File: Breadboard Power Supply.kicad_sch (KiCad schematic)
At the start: 29 parts, among them J1 USB-C, J10 Conn_01x02_Male, J11 Conn_01x02_Male, J2 Conn_02x03_Odd_Even, J3 Conn_02x03_Odd_Even, J8 Conn_01x02_Male, J9 Conn_01x02_Male, U1 LM1117-1.8, U2 LM1117-3.3

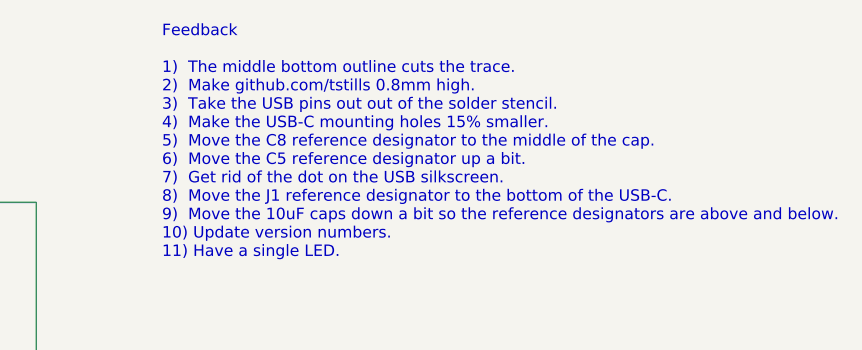
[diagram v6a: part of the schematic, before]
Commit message: Made the font for github.com/tstills larger.
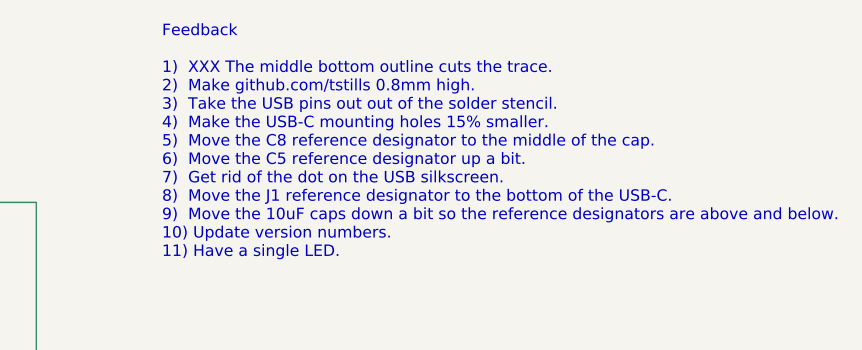
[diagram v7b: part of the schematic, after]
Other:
- note added: "Feedback 1) XXX The middle bottom outline cuts the trace. 2) Make github.com/tstills 0.8mm high. 3) Take the USB pins out out of the solder stencil. 4) Make the USB-C mounting holes 15% smaller. 5) Move the C8 reference designator to the middle of the cap. 6) Move the C5 reference designator up a bit. 7) Get rid of the dot on the USB silkscreen. 8) Move the J1 reference designator to the bottom o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"
- note removed: "Feedback 1) The middle bottom outline cuts the trace. 2) Make github.com/tstills 0.8mm high. 3) Take the USB pins out out of the solder stencil. 4) Make the USB-C mounting holes 15% smaller. 5) Move the C8 reference designator to the middle of the cap. 6) Move the C5 reference designator up a bit. 7) Get rid of the dot on the USB silkscreen. 8) Move the J1 reference designator to the bottom of th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"
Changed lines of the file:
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@@
     (effects (font (size 1.27 1.27)) (justify left bottom))
   )
-  (text "Feedback\n\n1)  The middle bottom outline cuts the trace.\n2)  Make github.com/tstills 0.8mm high.\n3)  Take the USB pins out out of the solder stencil.\n4)  Make the USB-C mounting holes 15% smaller.\n5)  Move the C8 reference designator to the middle of the cap.\n6)  Move the C5 reference designator up a bit.\n7)  Get rid of the dot on the USB silkscreen.\n8)  Move the J1 reference designator to the bottom of the USB-C.\n9)  Move the 10uF caps down a bit so the reference designators are above and below.\n10) Update version numbers.\n11) Have a single LED."
+  (text "Feedback\n\n1)  XXX The middle bottom outline cuts the trace.\n2)  Make github.com/tstills 0.8mm high.\n3)  Take the USB pins out out of the solder stencil.\n4)  Make the USB-C mounting holes 15% smaller.\n5)  Move the C8 reference designator to the middle of the cap.\n6)  Move the C5 reference designator up a bit.\n7)  Get rid of the dot on the USB silkscreen.\n8)  Move the J1 reference designator to the bottom of the USB-C.\n9)  Move the 10uF caps down a bit so the reference designators are above and below.\n10) Update version numbers.\n11) Have a single LED."
     (at 177.8 41.91 0)
     (effects (font (size 1.27 1.27)) (justify left bottom))

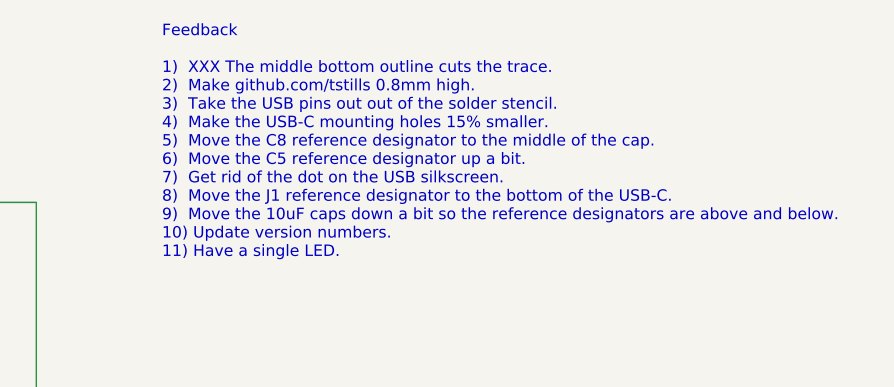
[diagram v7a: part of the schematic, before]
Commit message: Made the USB mounting holes 10% smaller.
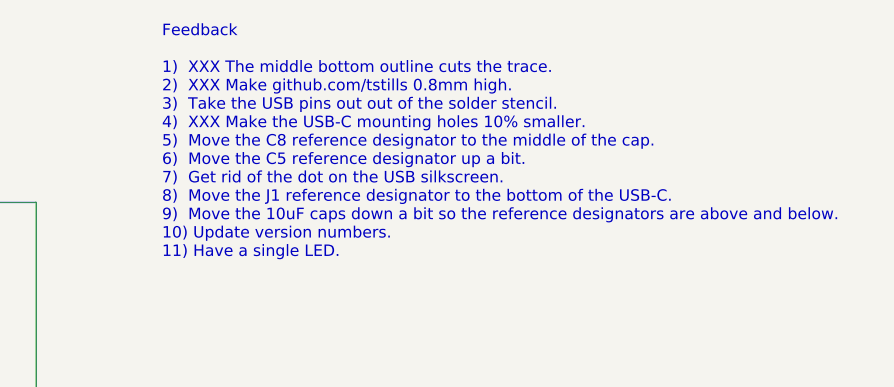
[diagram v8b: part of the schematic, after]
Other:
- note added: "Feedback 1) XXX The middle bottom outline cuts the trace. 2) XXX Make github.com/tstills 0.8mm high. 3) Take the USB pins out out of the solder stencil. 4) XXX Make the USB-C mounting holes 10% smaller. 5) Move the C8 reference designator to the middle of the cap. 6) Move the C5 reference designator up a bit. 7) Get rid of the dot on the USB silkscreen. 8) Move the J1 reference designator to the 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"
- note removed: "Feedback 1) XXX The middle bottom outline cuts the trace. 2) Make github.com/tstills 0.8mm high. 3) Take the USB pins out out of the solder stencil. 4) Make the USB-C mounting holes 15% smaller. 5) Move the C8 reference designator to the middle of the cap. 6) Move the C5 reference designator up a bit. 7) Get rid of the dot on the USB silkscreen. 8) Move the J1 reference designator to the bottom o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"
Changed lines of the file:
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@@
     (effects (font (size 1.27 1.27)) (justify left bottom))
   )
-  (text "Feedback\n\n1)  XXX The middle bottom outline cuts the trace.\n2)  Make github.com/tstills 0.8mm high.\n3)  Take the USB pins out out of the solder stencil.\n4)  Make the USB-C mounting holes 15% smaller.\n5)  Move the C8 reference designator to the middle of the cap.\n6)  Move the C5 reference designator up a bit.\n7)  Get rid of the dot on the USB silkscreen.\n8)  Move the J1 reference designator to the bottom of the USB-C.\n9)  Move the 10uF caps down a bit so the reference designators are above and below.\n10) Update version numbers.\n11) Have a single LED."
+  (text "Feedback\n\n1)  XXX The middle bottom outline cuts the trace.\n2)  XXX Make github.com/tstills 0.8mm high.\n3)  Take the USB pins out out of the solder stencil.\n4)  XXX Make the USB-C mounting holes 10% smaller.\n5)  Move the C8 reference designator to the middle of the cap.\n6)  Move the C5 reference designator up a bit.\n7)  Get rid of the dot on the USB silkscreen.\n8)  Move the J1 reference designator to the bottom of the USB-C.\n9)  Move the 10uF caps down a bit so the reference designators are above and below.\n10) Update version numbers.\n11) Have a single LED."
     (at 177.8 41.91 0)
     (effects (font (size 1.27 1.27)) (justify left bottom))
